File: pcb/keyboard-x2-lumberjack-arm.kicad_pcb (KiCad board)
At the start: 2 copper layers, 285 x 94.2 mm, 142 parts, among them J1 USB_C_Receptacle_USB2.0, U1 BluePill_or_MiniF4_DIP40, U2 SN74LVC1T45DBV

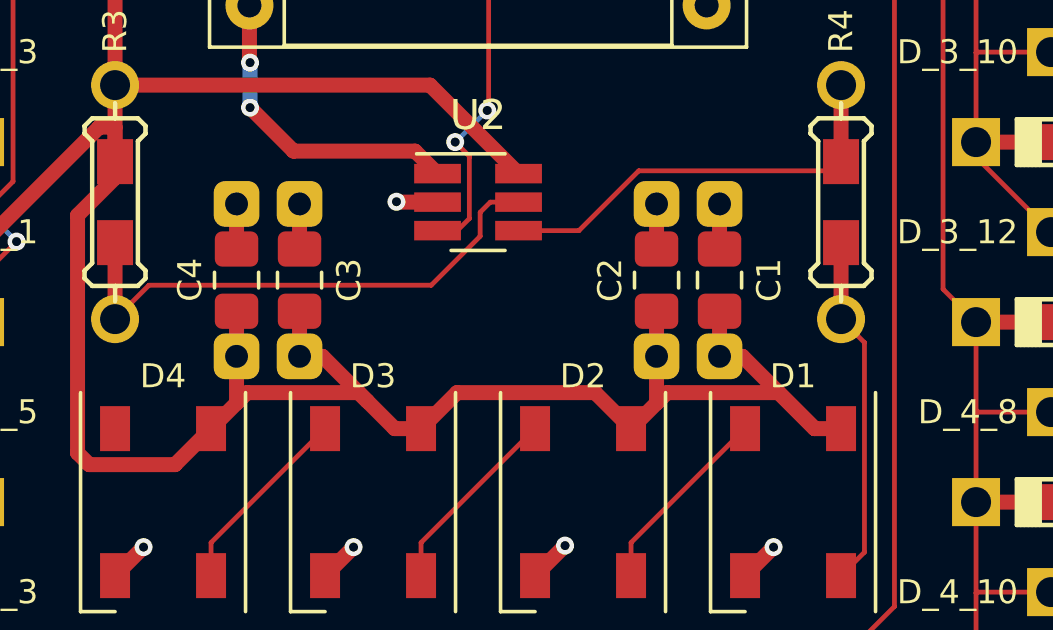
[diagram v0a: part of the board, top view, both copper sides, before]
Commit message: Kicad: update X-2 with details for generating an interactive BOM
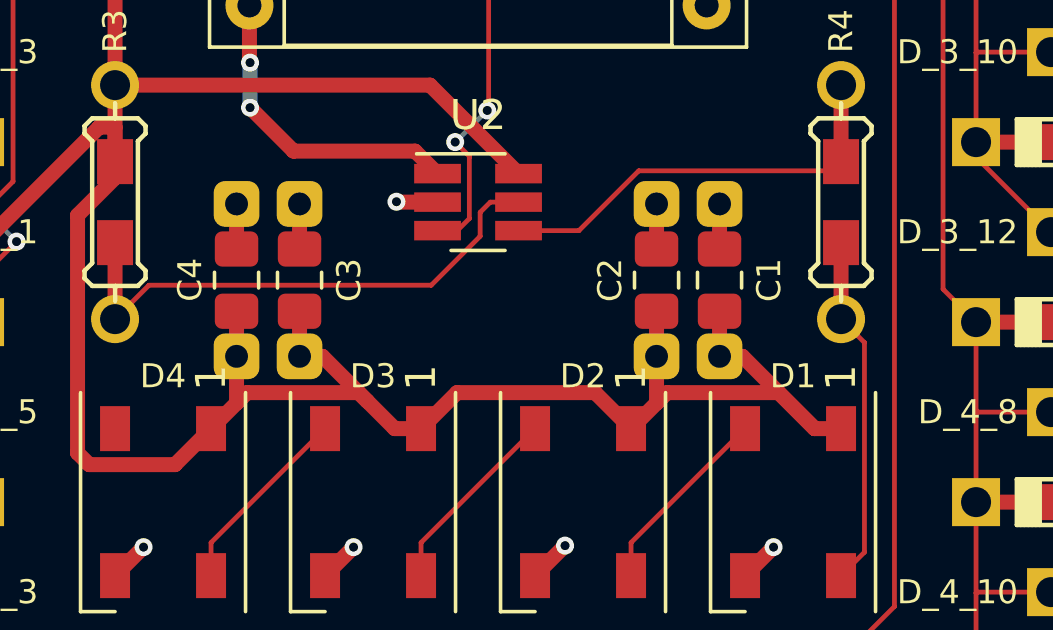
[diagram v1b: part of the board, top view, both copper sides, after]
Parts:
- D1, D2, D3, D4: value WS2812B -> SK6812
- D5, D_1_1, D_1_10, D_1_11, D_1_12, D_1_2, D_1_3, D_1_4, D_1_5, D_1_6, D_1_7, D_1_8, D_1_9, D_2_1, D_2_10, D_2_11, D_2_12, D_2_2, D_2_3, D_2_4, D_2_5, D_2_6, D_2_7, D_2_8, D_2_9, D_3_1, D_3_10, D_3_11, D_3_12, D_3_2, D_3_3, D_3_4, D_3_5, D_3_6, D_3_7, D_3_8, D_3_9, D_4_1, D_4_10, D_4_11, D_4_12, D_4_2, D_4_3, D_4_4, D_4_5, D_4_6, D_4_7, D_4_8, D_4_9, D_5_1, D_5_10, D_5_11, D_5_12, D_5_2, D_5_3, D_5_4, D_5_5, D_5_6, D_5_7, D_5_8, D_5_9: value D -> 1N4148
- H1, H2, H3, H4: value MountingHole -> M2 16mm Spacer
- H7: value MountingHole -> ~
- J1: value USB_C_Receptacle_USB2.0 -> 16-pin USB-C Connector SMD
- R1, R2: value R -> 5.1K
- SW_1_1, SW_1_10, SW_1_11, SW_1_12, SW_1_2, SW_1_3, SW_1_4, SW_1_5, SW_1_6, SW_1_7, SW_1_8, SW_1_9, SW_2_1, SW_2_10, SW_2_11, SW_2_12, SW_2_2, SW_2_3, SW_2_4, SW_2_5, SW_2_6, SW_2_7, SW_2_8, SW_2_9, SW_3_1, SW_3_10, SW_3_11, SW_3_12, SW_3_2, SW_3_3, SW_3_4, SW_3_5, SW_3_6, SW_3_7, SW_3_8, SW_3_9, SW_4_1, SW_4_10, SW_4_11, SW_4_12, SW_4_2, SW_4_3, SW_4_4, SW_4_5, SW_4_6, SW_4_7, SW_4_8, SW_4_9, SW_5_1, SW_5_10, SW_5_11, SW_5_12, SW_5_2, SW_5_3, SW_5_4, SW_5_5, SW_5_6, SW_5_7, SW_5_8, SW_5_9: value SW_Push -> MX-compatible or Kailh Choc v1
- U1: value BluePill_or_MiniF4_DIP40 -> DIP-40 round-pin socket or 40-pin SIP round-pin female header (cut down to 20)
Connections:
- J1 pad S1: (no net) -> Net-(J1-PadS1)

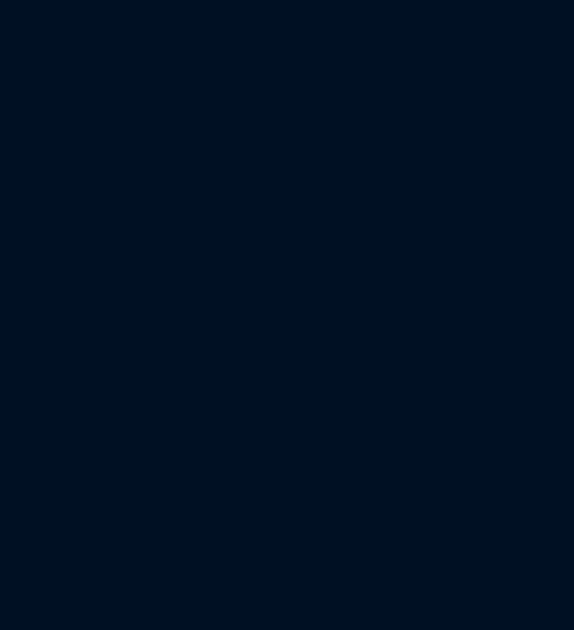
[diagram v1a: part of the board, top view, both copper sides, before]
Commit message: Kicad: update fields in X-1, X-2 for U1
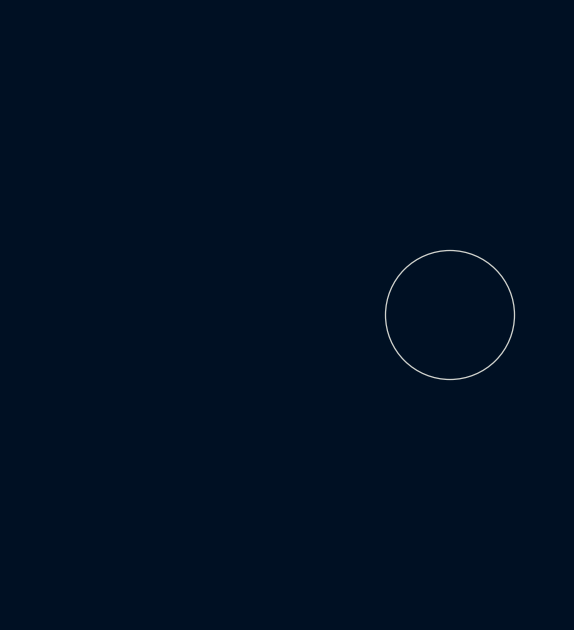
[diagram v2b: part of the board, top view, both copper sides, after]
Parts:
- added H5: ~, ProjectLocal:Bumpon_3M_F0502, F.Cu at (994.4, 83.1)
- added H6: ~, ProjectLocal:H_M2_Spacer_Hole, F.Cu at (1000.1, 82.7)
- U1: value DIP-40 round-pin socket or 40-pin SIP round-pin female header (cut down to 20) -> MiniF4 STM32F4x1 "Blackpill", or Bluepill

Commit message: Kicad: minor changes to silkscreen in X-2
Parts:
- REF**: moved to B.Cu
- turned REF** to 180 degrees
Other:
- board text added: "5V"
- board text added: "An Adaptation of u/peej's"
- board text added: "GND"
- board text added: "USB D+"
- board text added: "USB D-"
- board text removed: "An Adaption of u/peej's"

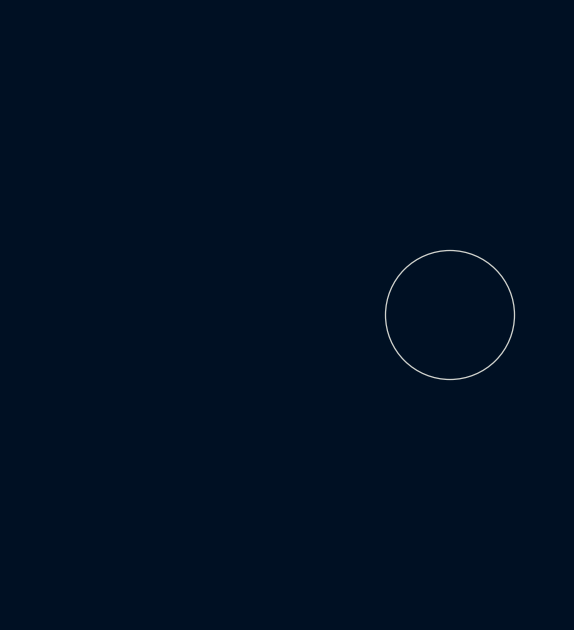
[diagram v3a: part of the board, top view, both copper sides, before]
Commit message: Kicad: remove unnecessary modules
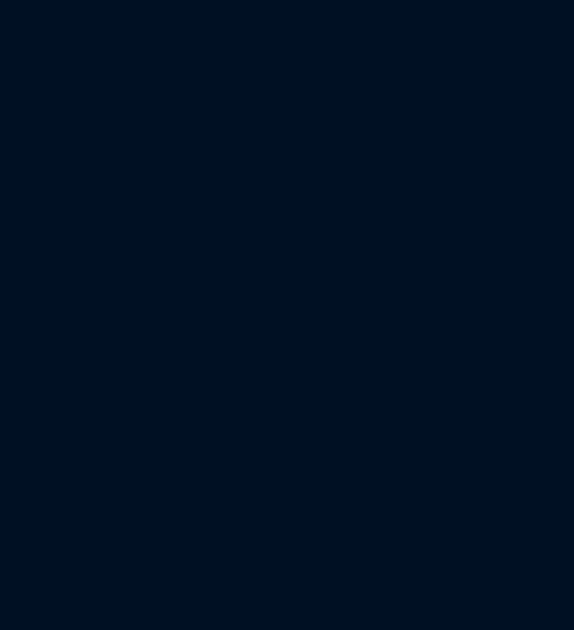
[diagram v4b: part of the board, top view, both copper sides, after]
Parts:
- removed H5: ~, ProjectLocal:Bumpon_3M_F0502
- removed H6: ~, ProjectLocal:H_M2_Spacer_Hole

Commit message: Kicad: re-add fancy cu/mask around where HOLES A, F were
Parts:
- added REF**: Graphic_Mask_HalfHole, ProjectLocal:Graphic_Mask_HalfHole, F.Cu at (331.3, 106.5)
- added REF**: Graphic_Mask_HalfHole, ProjectLocal:Graphic_Mask_HalfHole, F.Cu at (53.7, 106.5)
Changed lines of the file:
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@@
     (tracks 1419)
     (zones 0)
-    (modules 142)
+    (modules 144)
     (nets 112)
   )
@@
     (add_net VBUS)
   )
+  (module ProjectLocal:Graphic_Mask_HalfHole (layer F.Cu)
+    (at 331.2912 106.5 180)
+    (fp_text reference REF** (at 4.318 -2.54) (layer F.SilkS) hide
+      (effects (font (size 1 1) (thickness 0.15)))
+    )
+    (fp_text value Graphic_Mask_HalfHole (at 0 3.429) (layer F.Fab)
+      (effects (font (size 1 1) (thickness 0.15)))
+    )
+    (fp_line (start 0 -1.875) (end -3.7089 -1.875) (layer F.Mask) (width 1.25))
+    (fp_line (start -3.7089 1.875) (end 0 1.875) (layer F.Mask) (width 1.25))
+    (fp_line (start 0 -1.875) (end -3.7089 -1.875) (layer F.Cu) (width 1.25))
+    (fp_line (start 0 -1.875) (end -3.7089 -1.875) (layer B.Cu) (width 1.25))
+    (fp_line (start 0 -1.875) (end -3.7089 -1.875) (layer B.Mask) (width 1.25))
+    (fp_line (start -3.7089 1.875) (end 0 1.875) (layer F.Cu) (width 1.25))
+    (fp_line (start -3.7089 1.875) (end 0 1.875) (layer B.Cu) (width 1.25))
+    (fp_line (start -3.7089 1.875) (end 0 1.875) (layer B.Mask) (width 1.25))
+    (fp_arc (start 0 0) (end 0 1.875) (angle -180) (layer F.Mask) (width 1.25))
+    (fp_arc (start 0 0) (end 0 1.875) (angle -180) (layer F.Cu) (width 1.25))
+    (fp_arc (start 0 0) (end 0 1.875) (angle -180) (layer B.Cu) (width 1.25))
+    (fp_arc (start 0 0) (end 0 1.875) (angle -180) (layer B.Mask) (width 1.25))
+  )
+  (module ProjectLocal:Graphic_Mask_HalfHole (layer F.Cu)
+    (at 53.7089 106.5)
+    (fp_text reference REF** (at 4.318 -2.54) (layer F.SilkS) hide
+      (effects (font (size 1 1) (thickness 0.15)))
+    )
+    (fp_text value Graphic_Mask_HalfHole (at 0 3.429) (layer F.Fab)
+      (effects (font (size 1 1) (thickness 0.15)))
+    )
+    (fp_line (start -3.7089 1.875) (end 0 1.875) (layer B.Mask) (width 1.25))
+    (fp_line (start -3.7089 1.875) (end 0 1.875) (layer B.Cu) (width 1.25))
+    (fp_line (start -3.7089 1.875) (end 0 1.875) (layer F.Cu) (width 1.25))
+    (fp_line (start 0 -1.875) (end -3.7089 -1.875) (layer B.Mask) (width 1.25))
+    (fp_line (start 0 -1.875) (end -3.7089 -1.875) (layer B.Cu) (width 1.25))
+    (fp_line (start 0 -1.875) (end -3.7089 -1.875) (layer F.Cu) (width 1.25))
+    (fp_line (start -3.7089 1.875) (end 0 1.875) (layer F.Mask) (width 1.25))
+    (fp_line (start 0 -1.875) (end -3.7089 -1.875) (layer F.Mask) (width 1.25))
+    (fp_arc (start 0 0) (end 0 1.875) (angle -180) (layer B.Mask) (width 1.25))
+    (fp_arc (start 0 0) (end 0 1.875) (angle -180) (layer B.Cu) (width 1.25))
+    (fp_arc (start 0 0) (end 0 1.875) (angle -180) (layer F.Cu) (width 1.25))
+    (fp_arc (start 0 0) (end 0 1.875) (angle -180) (layer F.Mask) (width 1.25))
+  )
   (module lumberjack:OSHW (layer B.Cu)
